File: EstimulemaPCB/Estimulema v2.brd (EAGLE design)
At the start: 151 x 162 mm, 158 parts, among them IC3 74AC14N, IC4 ISO7240S, J1 JUMPERS12MM, J2 J15MM, J3 J_7MM, J4 JUMPERS5MM, J5 JUMPERS7MM, J6 J7MM, K2 HC-06, Q17 TIP48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

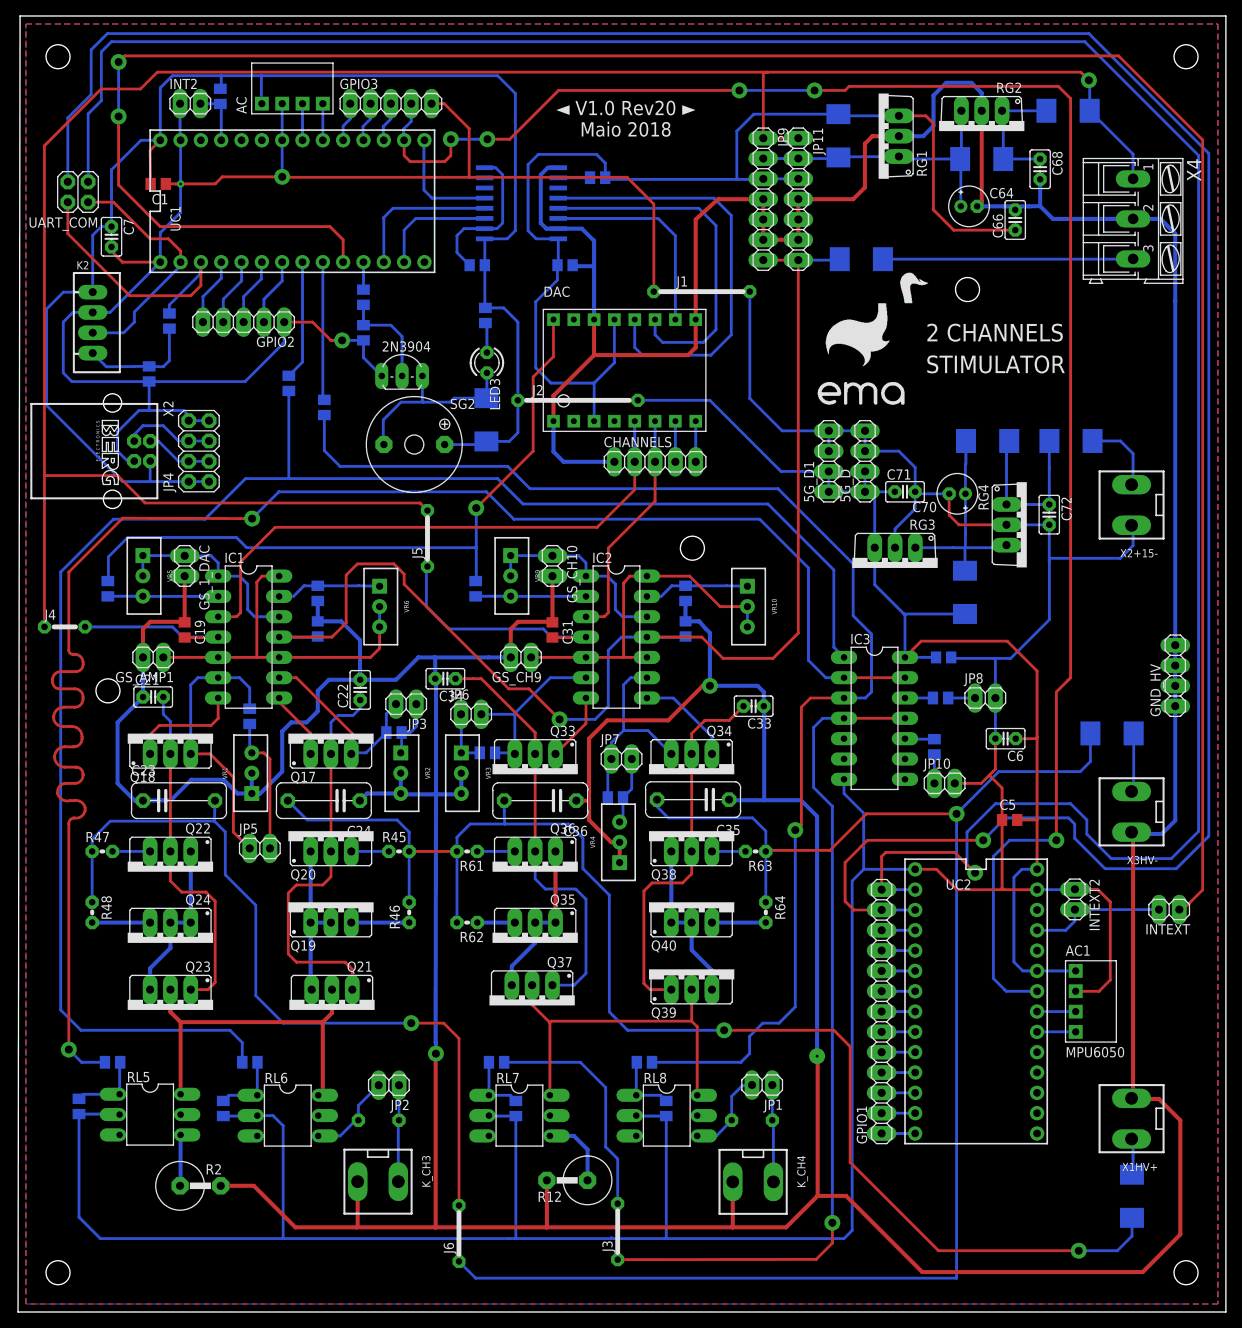
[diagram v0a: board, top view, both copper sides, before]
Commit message: final version working, teste OK!!
Updates:
1. Estimulema firmware: 
beep feature was remove of stim function
Cronaxie: this function was remove of firmware and instead it was placed the calibration function for activate the accelerate acquisition.

Other small fixes.

2. Accel firmware: updates in serial communications and add functions for data flow control

3. Add new version of firmware loadcell

4. add libraries used in inos firmware
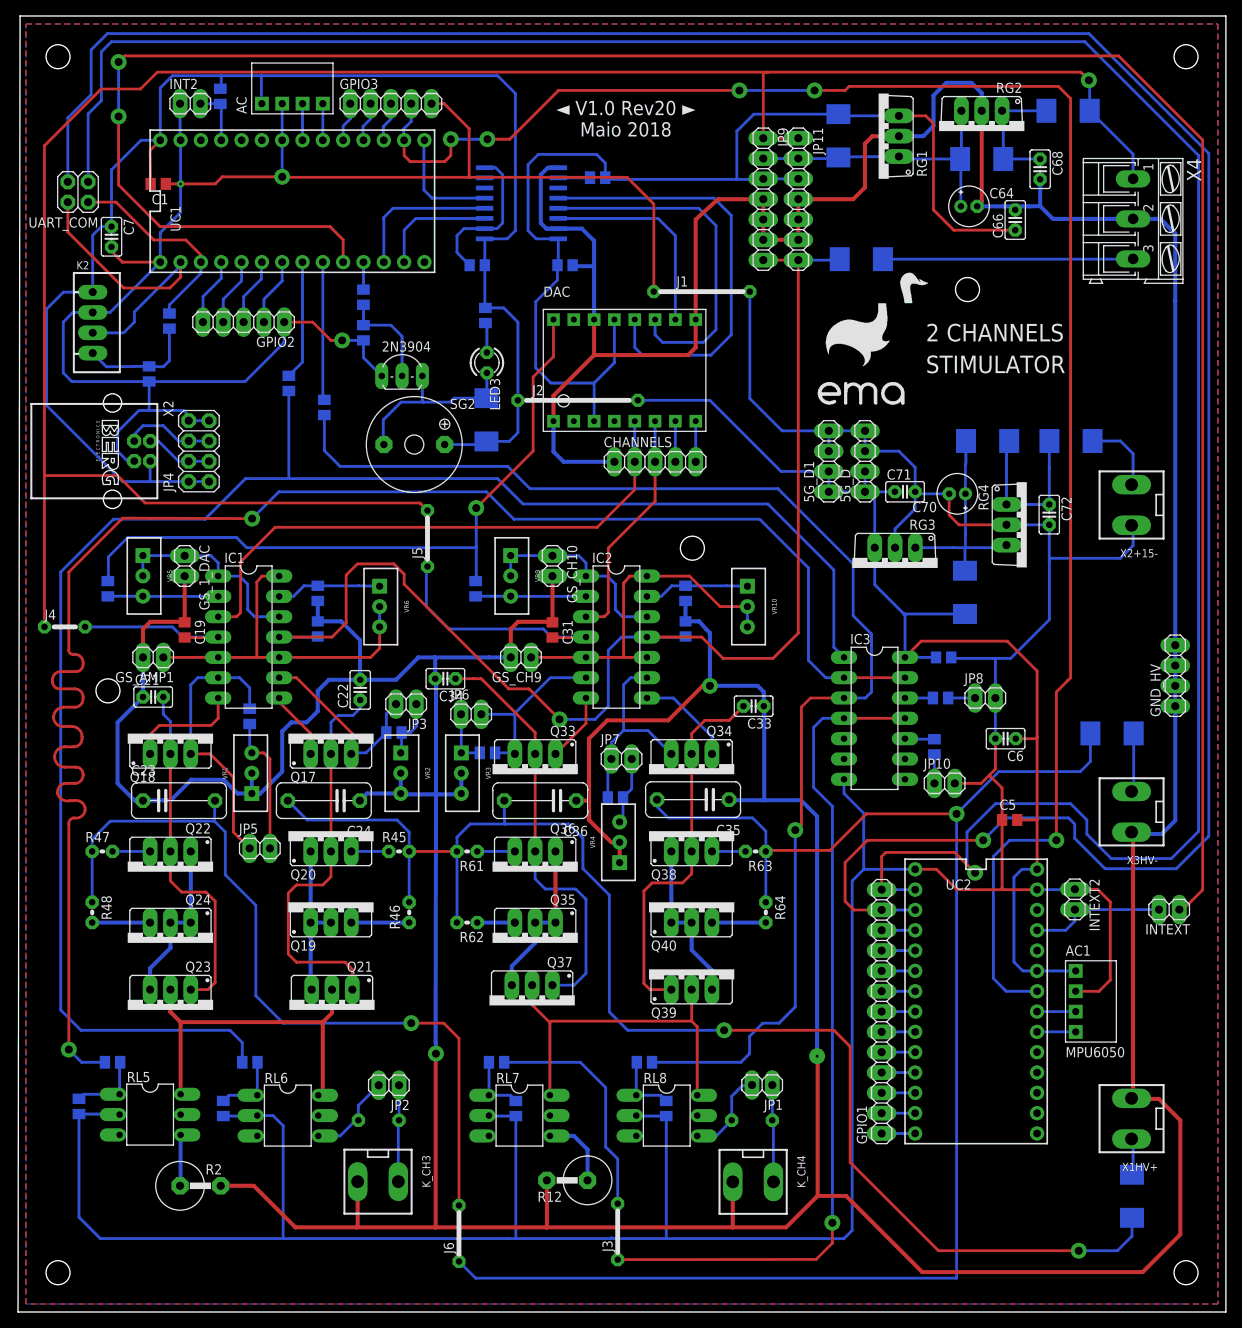
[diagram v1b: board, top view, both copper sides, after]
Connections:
- net N$36: now also UART_COM.2; no longer UART_COM.4
- net N$38: now also UART_COM.4; no longer UART_COM.2
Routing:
- net N$36: track 35.3 -> 25.8 mm
- net N$38: track 31.1 -> 38.8 mm
